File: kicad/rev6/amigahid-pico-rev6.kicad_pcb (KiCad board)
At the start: 2 copper layers, 100 x 80 mm, 115 parts, among them J1 A500 KBD OUT, J10 PS/2 KBD OUT, J11 DIN5 KBD IN, J12 PS/2 KBD IN, J13 USB-C AUX 5V, J2 DEBUG UART+SWD, J3 OLED I2C, J4 USB-A HOST, J7 SPARE GP28, J8 A500 KBD IN, J9 DIN5 KBD OUT, P1 DE9 MALE PORT 1, P2 DE9 MALE PORT 2, Q1 BSS138, Q10 BSS138, Q11 BSS138, Q12 BSS138, Q13 BSS138, Q14 BSS138, Q15 BSS138, Q16 BSS138, Q17 BSS138, Q18 BSS138, Q19 BSS138, Q2 BSS138, Q3 BSS138, Q4 BSS138, Q5 BSS138, Q6 BSS138, Q7 BSS138, Q8 BSS138, Q9 BSS138, U1 PicoW, U2 USBLC6-2SC6

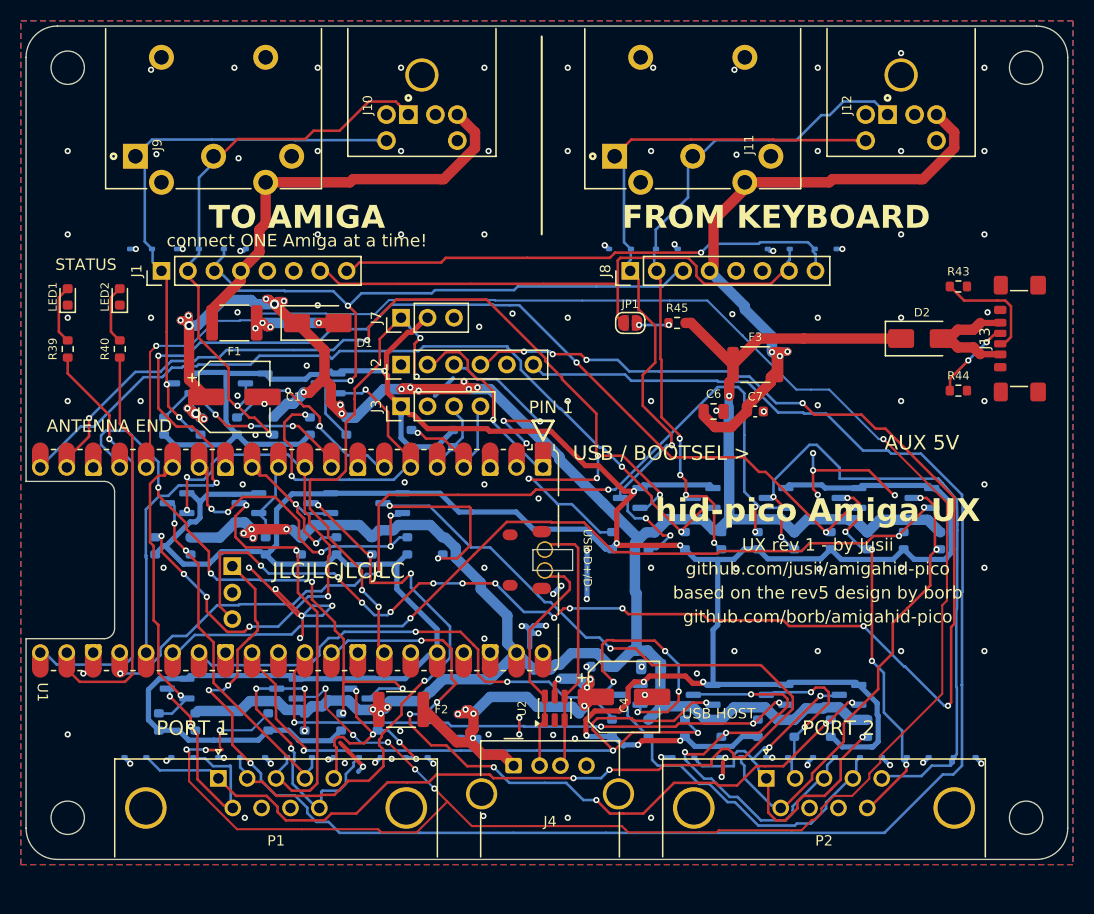
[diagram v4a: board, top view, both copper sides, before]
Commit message: kicad: retarget the de9 land to the .318in family
the rev6 DE9 land only ever matched Power Dynamics PDI-09S-5: a 5.34 mm
footprint with its boardlock holes collinear with the near pin row, which
is a PDI-proprietary trait, and the part is dead and unobtainable.  retarget
P1/P2 to the industry .318in/8.08 mm family, whose boardlock holes sit
midway between the pin rows.  primary buy is Kycon K22X-E9P-N; NorComp
182-009-113R531, TE 5747840-x, Wurth 618009231221 and Amphenol L717 code
33E are drop-in.

  * footprint renamed to the stock KiCad variant name
    EdgePinOffset7.70mm_Housed_MountingHolesOffset9.12mm, with its
    drawing taken from that variant: body, flange and boardlock legs all
    2.76 mm further from the pin rows.  the silk rails stop at local
    y=10.15 rather than the stock 10.48 so 0.15 mm silk clearance holds
    against the board edge.
  * pin coordinates unchanged - every D-sub family shares them - but the
    18 pin drills open 1.0 -> 1.1 mm for the 1.09 mm Kycon pin.  annulus
    stays 0.25 mm, well over the 0.13 mm floor.
  * the four boardlock pads move from local y=2.84 to y=1.42, i.e. from
    the near pin row to midway between the rows.  they stay 3.2 mm drill
    / 4.0 mm pad, plated, on GND with a solid zone connection.
  * south board edge moves 80.00 -> 82.76 so the near pin row sits the
    family's 7.70 mm behind it; the two south corner arcs and the side
    rails follow, and the south M3 holes keep their 4 mm corner inset at
    (4,78.76) and (96,78.76).  both GND pours extend to y=83.26.
  * re-routed around the moved boardlocks: /cont1_v and /cont1_b2_lo at
    P1 east, /cont2_v_lo, /cont2_vq and /cont2_hq at P2 west, /swclk at
    P2 east (which now hops to F.Cu to get past /cont2_b3).  no component
    moved.
  * the wider pin drills cost 0.05 mm of hole clearance, which the runs
    threading the two pin fields did not have; 30 runs slide 0.02-0.05 mm
    to re-centre in their corridors, and a 0.07 mm router spike on
    /co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
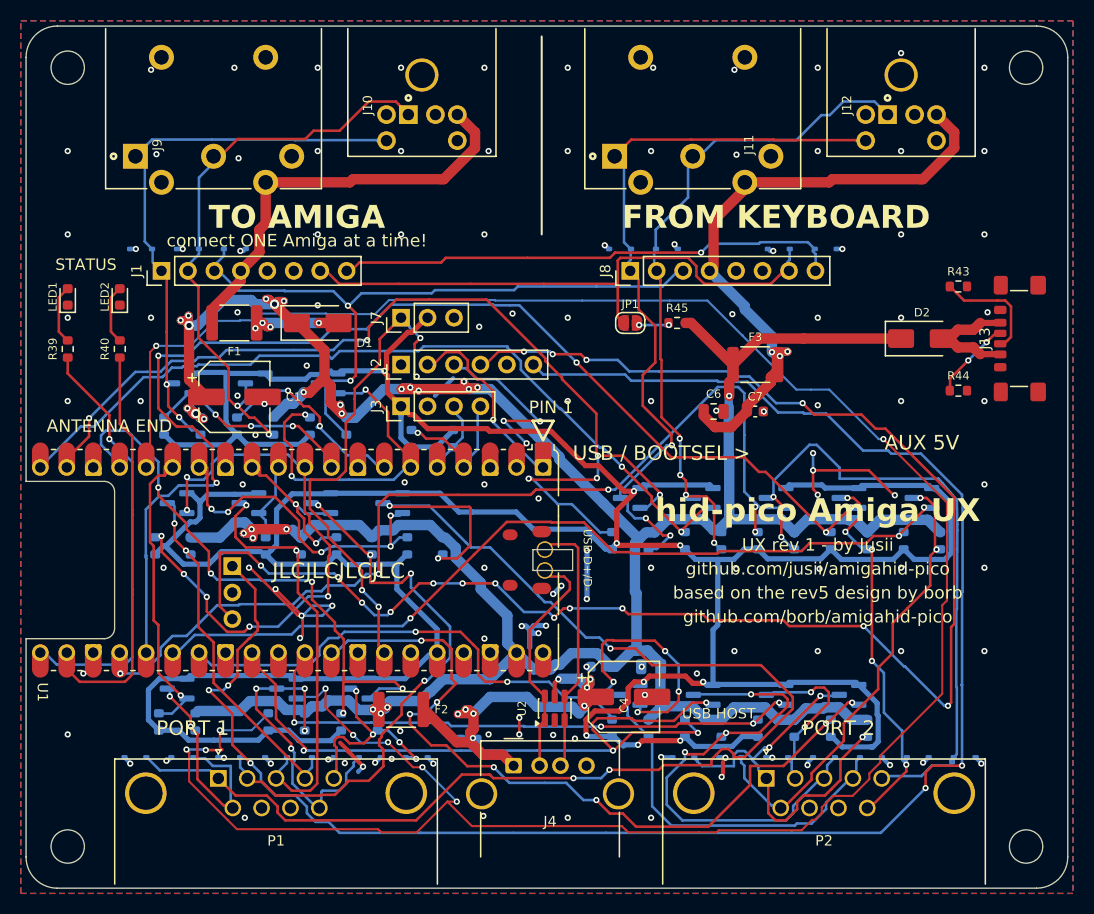
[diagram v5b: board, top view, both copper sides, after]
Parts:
- P1, P2: footprint rev6:DSUB-9_Pins_Horizontal_P2.77x2.84mm_EdgePinOffset4.94mm_Housed_MountingHolesOffset4.94mm -> rev6:DSUB-9_Pins_Horizontal_P2.77x2.84mm_EdgePinOffset7.70mm_Housed_MountingHolesOffset9.12mm
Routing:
- net /cont2_vq: track 40.0 -> 45.1 mm
- net /cont2_hq: track 31.7 -> 34.3 mm
- net /cont2_v_lo: track 72.0 -> 73.8 mm
- net /cont1_b2_lo: track 232.0 -> 233.9 mm
- net /swclk: track 171.2 -> 172.2 mm, vias 3 -> 5
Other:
- board size 100 x 80 mm -> 100 x 82.8 mm

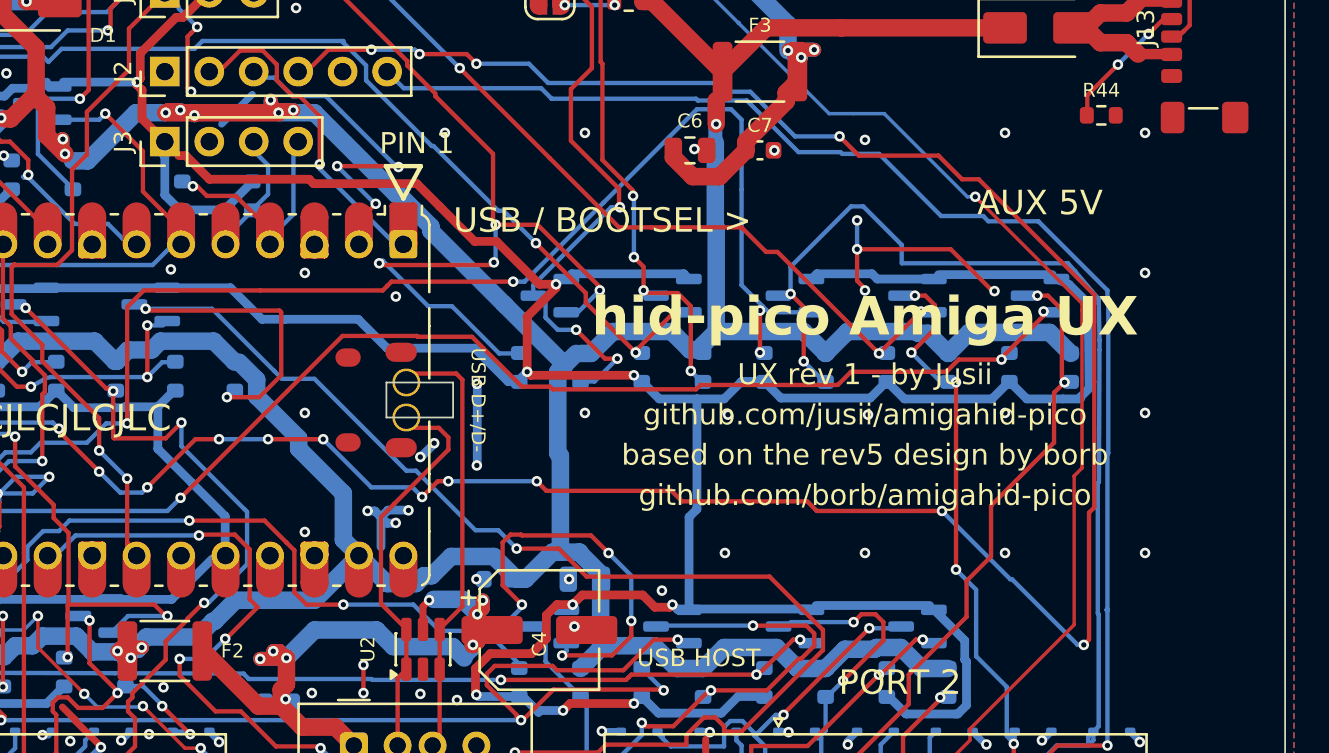
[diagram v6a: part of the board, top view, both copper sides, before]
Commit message: kicad: mount the oled on a socket and two posts
the 0.96in ssd1306 module now plugs straight down onto the board instead of
hanging off wires: J3 becomes a 1x4 female socket at the module's header edge
(pins x 81.74-89.36, y 40.5) and two M2 posts hold the east edge, H1 (97.3,
40.5) and H2 (97.3, 64.3), 2.2 mm NPTH, board-only footprints.  the module
sits at x 71.8-99.3, y 38.5-66.3, flush inside the east edge.  the other two
corners get no post on purpose: the lower-left one lands on Q18 and six
port-2 nets, the upper-left one sits in the corridor the i2c pair crosses.

  * J3's pin order is the module's, GND VCC SCL SDA, so pins 1 and 2 swap
    nets in the schematic (was 3V3 GND SCL SDA); footprint and Sourcing
    field follow.  a VCC-GND module wants the two labels swapped back.
  * the i2c pair leaves the pico through the lane the redundant +3V3 F.Cu
    loop occupied (the pocket's pull-ups and J7 are fed from the west, via a
    via at the old J3 pad-1 spot and one link down to the pico-side +3V3),
    then 45 mm east to the socket.  /swclk, /swdio and /cont1_b2_lo, which
    ran through the new pad row, are re-threaded north of it.  three GND
    stitch vias re-link pour patches the new lanes walled off.
  * the credit block moves to the bottom silkscreen (the module covers its
    old spot); "AUX 5V" shifts north clear of the module edge.
  * check_rev6_netlist.py: J3 map RE-TARGETED to the socket's pin order
    (1 = gnd, 2 = 3v3); 357/357, nothing relaxed.  check_rev6_pcb.py pins
    the new blob; the commit hash is pinned in the follow-up.
  * doc/errata.md, the mouser bom and the order list carry the mount:
    post length = socket body + 2.54 mm (11 mm for an 8.5 mm socket), never
    under 8 mm because the pico's micro-usb cable passes under the module's
    west edge.

gates: erc 0; drc 0 violations / 0 unconnected / 0 parity; check_rev6_netlist.py
357/357; check_rev6_style.py S1 99.8%, S2 0 staircases, S3 clean;
check_rev6_pcb.py 37/38 - J3 red only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
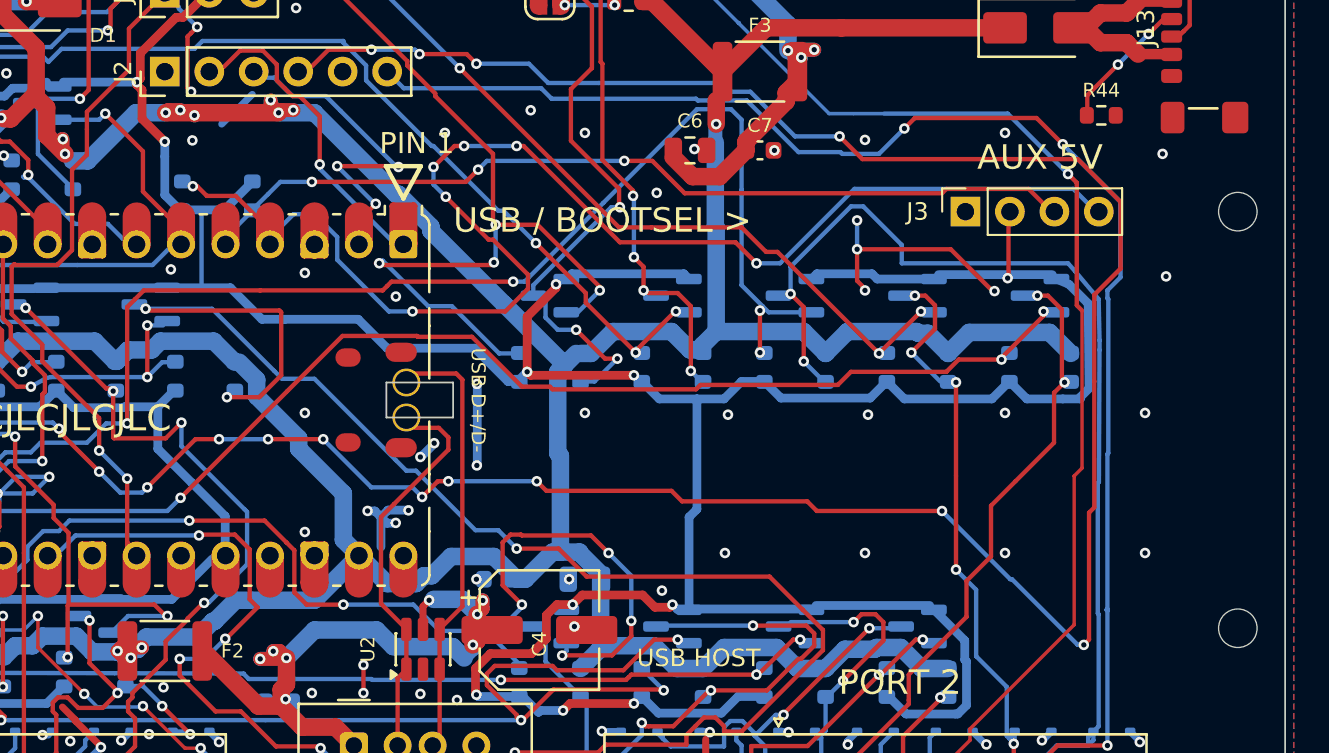
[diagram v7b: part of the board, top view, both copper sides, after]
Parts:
- added H1: M2 OLED post, MountingHole:MountingHole_2.2mm_M2, F.Cu at (97.3, 40.5)
- added H2: M2 OLED post, MountingHole:MountingHole_2.2mm_M2, F.Cu at (97.3, 64.3)
- J3: footprint Connector_PinHeader_2.54mm:PinHeader_1x04_P2.54mm_Vertical -> Connector_PinSocket_2.54mm:PinSocket_1x04_P2.54mm_Vertical
- moved J3 45.9 mm to (81.7, 40.5)
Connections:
- J3 pad 1: +3V3 -> GND
- J3 pad 2: GND -> +3V3
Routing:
- net /i2c_sda: track 10.7 -> 77.3 mm, vias 1 -> 7
- net /i2c_scl: track 5.40 -> 50.1 mm, vias 0 -> 3
- net +3V3: track 361.5 -> 346.4 mm, vias 9 -> 11
- net /swclk: track 172.2 -> 177.9 mm, vias 5 -> 7
- net /swdio: track 157.3 -> 162.6 mm
- net /cont1_b2_lo: track 233.9 -> 237.7 mm
- net GND: vias 127 -> 130
